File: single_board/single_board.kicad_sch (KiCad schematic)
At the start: 121 parts, among them J11 SPI Debug, J17 BOOTSEL, J18 Power, J2 USB_C_Receptacle_USB2.0_16P, J3 SWD, J30 JST_GH_H, J31 JST_GH_H, J33 JST_GH_H, J34 PB_Vertical, J35 JST_GH_H, J36 JST_GH_H, J37 JST_GH_H, J38 PB_Vertical, J39 PB_Vertical, J40 PB_Vertical, J41 PB_Vertical, J42 PB_Vertical, J43 PB_Vertical, J44 PB_Vertical, J45 PB_Vertical, J46 PB_Vertical, J47 PB_Vertical, J48 PB_Vertical, J49 PB_Vertical, J5 JST-GH, J50 PB_Vertical, J53 PB_Vertical, Q1 AO3400A, Q3 AO3401A, SW1 Button, U1 AP2112K-3.3, U3 USBLC6-2SC6, U4 LSM6DSV, U5 STM32G474VBTx, Y2 ABM8-16MHz

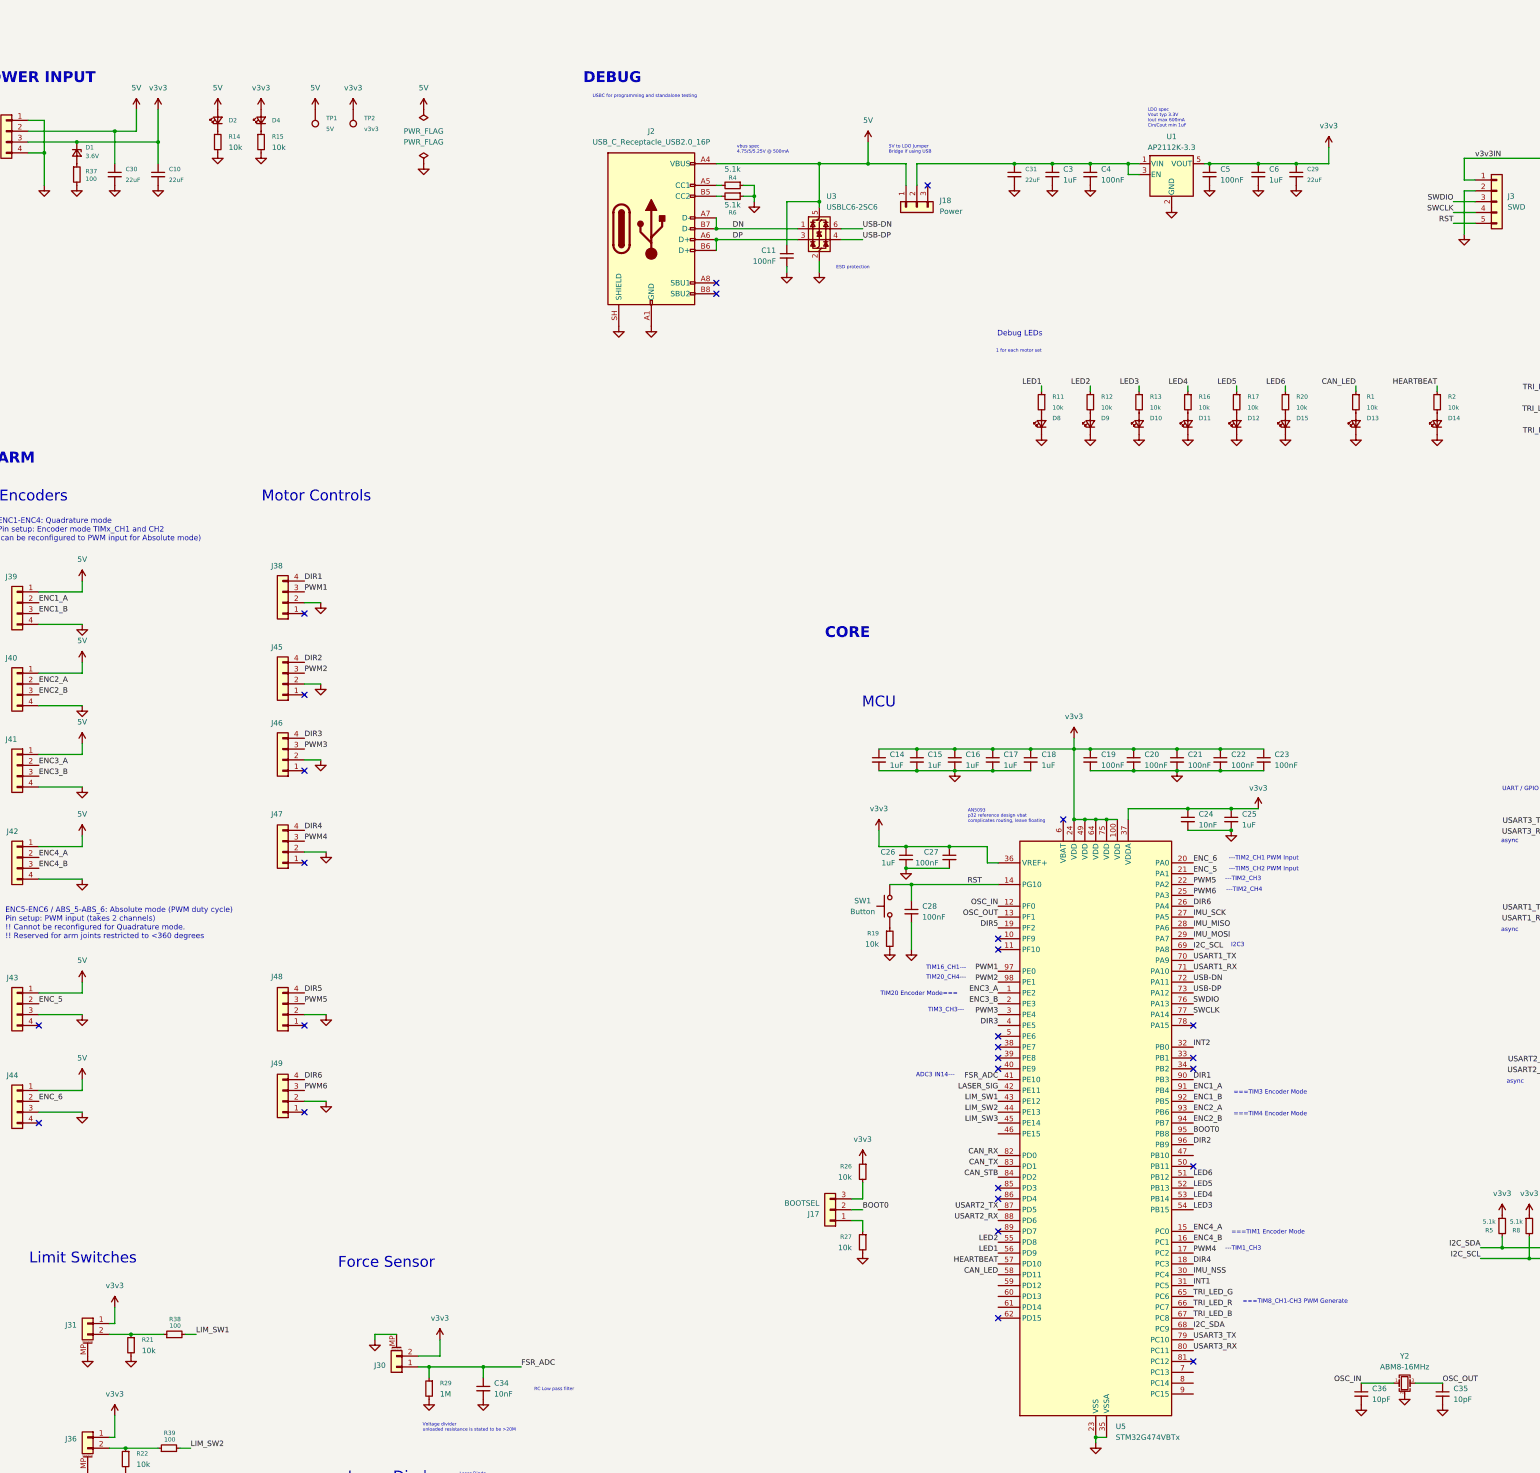
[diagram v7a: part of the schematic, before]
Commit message: Silkscreen on LEDs
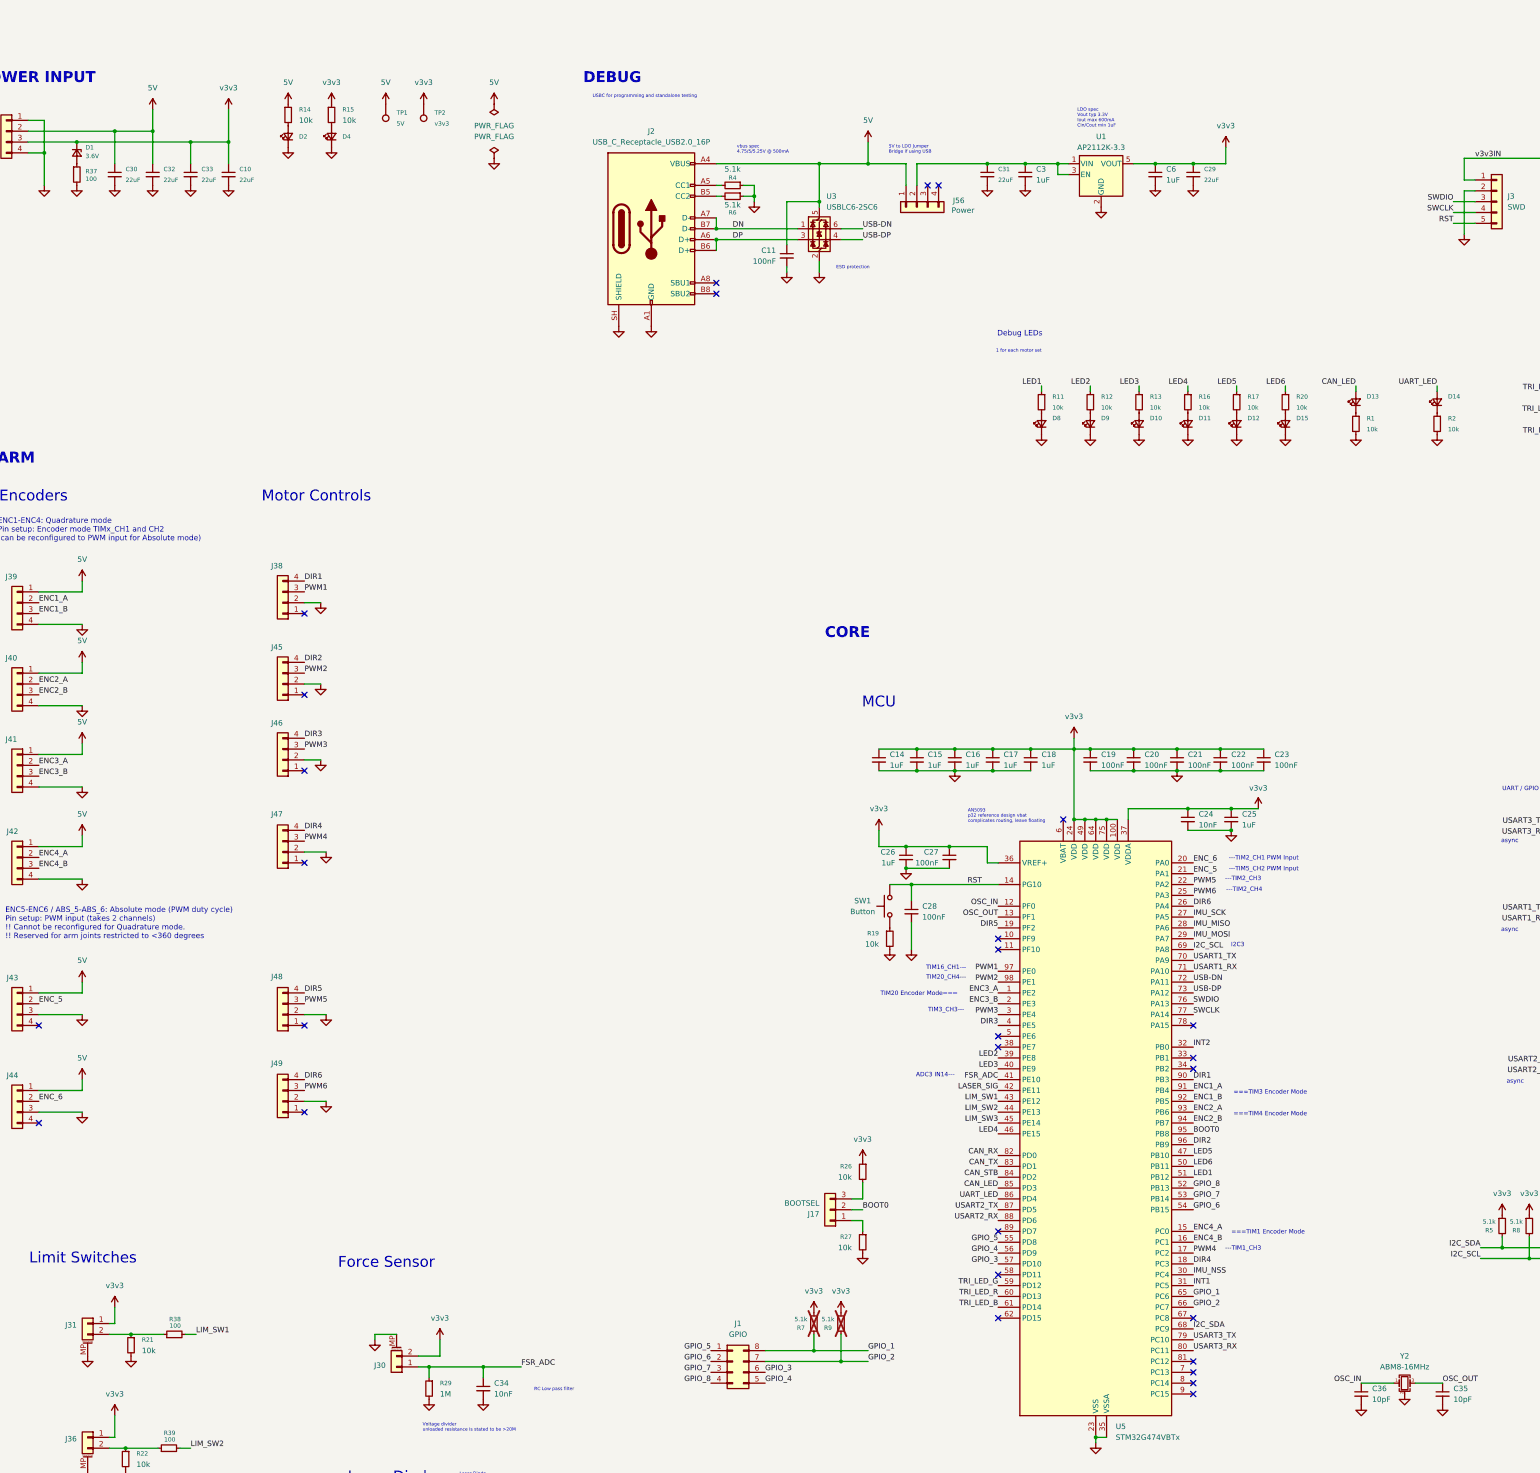
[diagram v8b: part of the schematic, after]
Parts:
- removed C4, C5: 100nF, Capacitor_SMD:C_0402_1005Metric, symbol Device:C_Small
- removed J18: Power, Connector_PinHeader_2.54mm:PinHeader_1x03_P2.54mm_Vertical, symbol Connector_Generic:Conn_01x03
- added C32, C33: 22uF, Capacitor_SMD:C_0805_2012Metric, symbol Device:C_Small
- added J1: GPIO, Connector_PinHeader_2.54mm:PinHeader_2x04_P2.54mm_Vertical, symbol Connector_Generic:Conn_02x04_Counter_Clockwise
- added J56: Power, Connector_PinHeader_2.54mm:PinHeader_1x04_P2.54mm_Vertical, symbol Connector_Generic:Conn_01x04
- added R7, R9: 5.1k, Resistor_SMD:R_0402_1005Metric, symbol Device:R_Small
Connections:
- net 5V: now also R14.1, C32.1, J56.1 (Pin_1); no longer D2.2 (A)
- net CAN_LED: now also D13.2 (A), U5.85 (PD3); no longer R1.1, U5.58 (PD11)
- net GND: now also D2.1 (K), D4.1 (K), R1.2, R2.2, C32.2, C33.2; no longer D13.1 (K), D14.1 (K), R14.2, R15.2
- net LED1: now also U5.51 (PB12); no longer U5.56 (PD9)
- net LED2: now also U5.39 (PE8); no longer U5.55 (PD8)
- net LED3: now also U5.40 (PE9); no longer U5.54 (PB15)
- net LED4: now also U5.46 (PE15); no longer U5.53 (PB14)
- net LED5: now also U5.47 (PB10); no longer U5.52 (PB13)
- net LED6: now also U5.50 (PB11); no longer U5.51 (PB12)
- net TRI_LED_B: now also U5.61 (PD14); no longer U5.67 (PC8)
- net TRI_LED_G: now also U5.59 (PD12); no longer U5.65 (PC6)
- net TRI_LED_R: now also U5.60 (PD13); no longer U5.66 (PC7)
- net v3v3: now also R15.1, C33.1, R7.1, R9.1; no longer D4.2 (A)
- net at C3.1, C31.1, U1.1 (VIN)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: now also J56.2 (Pin_2)
- net UART_LED: now reaches D14.2 (A)
- net UART_LED: now also U5.86 (PD4); no longer R2.2
- net HEARTBEAT: no longer names the net of R2.1
- net HEARTBEAT: now also D14.1 (K); no longer U5.57 (PD10)
- new net: D13.1 (K), R1.1
- new net: D2.2 (A), R14.2
- new net: D4.2 (A), R15.2
- new net GPIO_1: J1.8 (Pin_8), R7.2, U5.65 (PC6)
- new net GPIO_2: J1.7 (Pin_7), R9.2, U5.66 (PC7)
- new net GPIO_3: J1.6 (Pin_6), U5.57 (PD10)
- new net GPIO_4: J1.5 (Pin_5), U5.56 (PD9)
- new net GPIO_5: J1.1 (Pin_1), U5.55 (PD8)
- new net GPIO_6: J1.2 (Pin_2), U5.54 (PB15)
- new net GPIO_7: J1.3 (Pin_3), U5.53 (PB14)
- new net GPIO_8: J1.4 (Pin_4), U5.52 (PB13)
- no-connect marks 35 -> 36
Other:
- note removed: "===TIM8_CH1-CH3 PWM Generate"
- moved on the sheet: C10, C29, C3, C31, C6, D13, D14, D2, D4, R1, R14, R15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
